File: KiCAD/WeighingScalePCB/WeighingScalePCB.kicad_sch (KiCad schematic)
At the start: 42 parts, among them J1 Conn_01x04_Pin, Q1 MMBT2222A, Q2 BSS138, Q3 BSS138, T1 TouchPad, T2 TouchPad, U1 XIAO-ESP32-S3-SMD, U2 HX711, U3 SSD1306, U4 RT9193-33GB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

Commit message: updated connectors, added chip en circuit
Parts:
- removed C10, C13, C8, C9: 1uF, Capacitor_SMD:C_0402_1005Metric, symbol Device:C
- removed C11, C12, C14: 10uF, Capacitor_SMD:C_0402_1005Metric, symbol Device:C
- removed JP1: SolderJumper_2_Bridged, symbol Jumper:SolderJumper_2_Bridged
- removed Q2, Q3: BSS138, Package_TO_SOT_SMD:SOT-23, symbol Transistor_FET:BSS138
- removed R12: 1K, Resistor_SMD:R_0402_1005Metric, symbol Device:R_US
- removed U3: SSD1306, KiCad-SSD1306_OLED-0.91-128x32-master:SSD1306_OLED-0.91-128x32, symbol SSD1306_OLED-0.91-128x32:SSD1306
- removed U4: RT9193-33GB, RT9193-33GB:SOT94P279X129-5N, symbol RT9193-33GB:RT9193-33GB
- added C17: 0.1uF, Capacitor_SMD:C_0402_1005Metric, symbol Device:C
- added D1: SP720ABTG, SOIC127P600X175-16N, symbol ESD diode:SP720ABTG
- added IC1: MAX6675ISA+T, SOIC127P600X175-8N, symbol MAX6675ISA+T:MAX6675ISA+T
- added IC2: APS11753KMDALX-9PL5, SOT95P240X115-3N, symbol APS11753KMDALX-9PL5:APS11753KMDALX-9PL5
- added J2: AudioJack4, symbol Connector_Audio:AudioJack4
- added J3: CONN_14_FFC/FPC, symbol Connector_Generic_MountingPin:Conn_01x14_MountingPin
- added J4: Battery Conn, symbol Connector:Conn_01x02_Pin
- added JP2: SolderJumper_2_Open, symbol Jumper:SolderJumper_2_Open
- added JP3: rate setting, symbol Jumper:SolderJumper_3_Open
- added Q2, Q3: NX138AKR, SOT95P230X110-3N, symbol NX138AKR Mosfet:NX138AKR
- R10, R9: value 10K -> 200K
- R11: value 1K -> 200K
- R6: value 100 -> 200K
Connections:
- net 3.3V is gone; now on net VCC: R7.1, R8.1
- net DOut: now also U1.7 (GPIO16_D6_TX); no longer U1.2 (GPIO1_A1_D1)
- net GND: now also R10.2, R9.2, C17.1, D1.8 (V-), IC1.1 (GND), IC2.3 (GND), JP2.2 (B), JP3.2 (C); no longer R11.2, R6.2
- net PD_SCK: now also U1.11 (GPIO18_D10_MOSI); no longer U1.1 (GPIO0_A0_D0)
- net VCC: now also U1.12 (3V3), C17.2, D1.16 (V+), IC1.4 (VCC), IC2.1 (VCC); no longer R10.1, R11.1, R9.1, U1.14 (5V)
- net at R3.1: now also JP3.1 (A); no longer U2.15 (RATE)
- net SO: now reaches U1.10 (GPIO20_D9_MISO)
- net SO: now also IC1.7 (SO)
- net V_BAT: now reaches U1.15 (BAT)
- net V_BAT: now also R11.1, R6.1, J4.1 (Pin_1)
- net at U1.16 (GND): now also J4.2 (Pin_2)
- net enable: now reaches U1.19 (CHIP_EN)
- net enable: now also Q2.2 (S), Q3.2 (S)
- net CS_N: now reaches U1.8 (GPIO17_D7_RX)
- net CS_N: now also IC1.6 (~{CS})
- net SCK: now reaches U1.9 (GPIO19_D8_SCK)
- net SCK: now also IC1.5 (SCK)
- net SCL_3.3V renamed SCL
- net SCL: now also U1.6 (GPIO23_D5_SCL)
- removed net SCL_5V: R9.2, U1.6 (GPIO23_D5_SCL)
- net SDA_3.3V renamed SDA
- net SDA: now also U1.5 (GPIO22_D4_SDA)
- removed net SDA_5V: R10.2, U1.5 (GPIO22_D4_SDA)
- new net: IC1.2 (T-), J2.R2, J2.T
- new net: IC1.3 (T+), J2.R1, J2.S
- new net: IC1.8 (N.C.), JP2.1 (A)
- new net: Q2.3 (D), Q3.3 (D), R11.2
- new net: IC2.2 (VOUT), Q3.1 (G), R10.1
- new net: R6.2, R9.1, U1.1 (GPIO0_A0_D0)
- new net: JP3.3 (B), U2.15 (RATE)
- new net ble_keep_awake: Q2.1 (G), U1.2 (GPIO1_A1_D1)
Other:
- note added: "Add a circuit which outputs a trigger to operate buzzer for a specific time delay for every rising edge"
- note added: "MAX6675 ~ 0.3V - 6V"
- moved on the sheet: R3, R7, R8, T1, T2

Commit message: 1. Added buzzer beep implementation - to be reviewed and calculations to be finalised 2. cleaned up schematic 3. added comments of pending activities
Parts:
- added C8, C9: 22pF, Capacitor_SMD:C_0402_1005Metric, symbol Device:C
- added D2: D, symbol Device:D
- added Q4: NX138AKR, SOT95P230X110-3N, symbol NX138AKR Mosfet:NX138AKR
- added R12, R13: 200K, Resistor_SMD:R_0402_1005Metric, symbol Device:R_US
- added U3: NE555D, Package_SO:SOIC-8_3.9x4.9mm_P1.27mm, symbol Timer:NE555D
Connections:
- net Time is gone; now on net Tare: U1.4 (GPIO21_D3), U6.1 (Q)
- net GND: now also J3.MP (MountPin), C8.2, C9.2, Q4.2 (S), U3.1 (GND)
- net Tare: now also D2.2 (A)
- net VCC: now also R12.1, R13.2, U3.8 (VCC)
- net beep: now also U3.3 (Q)
- net at D1.1 (IN_1): now also J3.1 (Pin_1)
- net at D1.10 (IN_9): now also J3.9 (Pin_9)
- net at D1.11 (IN_10): now also J3.10 (Pin_10)
- net at D1.12 (IN_11): now also J3.11 (Pin_11)
- net at D1.13 (IN_12): now also J3.12 (Pin_12)
- net at D1.14 (IN_13): now also J3.13 (Pin_13)
- net at D1.15 (IN_14): now also J3.14 (Pin_14)
- net at D1.2 (IN_2): now also J3.2 (Pin_2)
- net at D1.3 (IN_3): now also J3.3 (Pin_3)
- net at D1.4 (IN_4): now also J3.4 (Pin_4)
- net at D1.5 (IN_5): now also J3.5 (Pin_5)
- net at D1.6 (IN_6): now also J3.6 (Pin_6)
- net at D1.7 (IN_7): now also J3.7 (Pin_7)
- net at D1.9 (IN_8): now also J3.8 (Pin_8)
- new net: D2.1 (K), Q4.1 (G)
- new net: R13.1, U3.4 (R)
- new net: C9.1, R12.2, U3.6 (THR), U3.7 (DIS)
- new net: Q4.3 (D), U3.2 (TR)
- new net: C8.1, U3.5 (CV)
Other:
- note added: "Load cell amplifier"
- note added: "OLED interface"
- note added: "Processor"
- note added: "Thermocouple amplifier"
- note added: "Touch pad input and buzzer"
- note added: "slide enable implementation"
- moved on the sheet: C1, C15, C16, C17, C2, C3, C4, C5, C6, C7, D1, IC1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

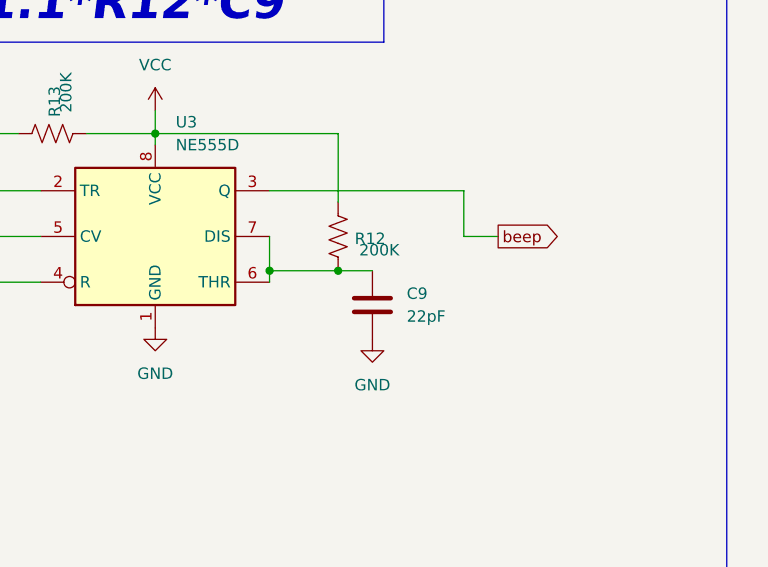
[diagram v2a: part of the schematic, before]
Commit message: Added half millisecond beep
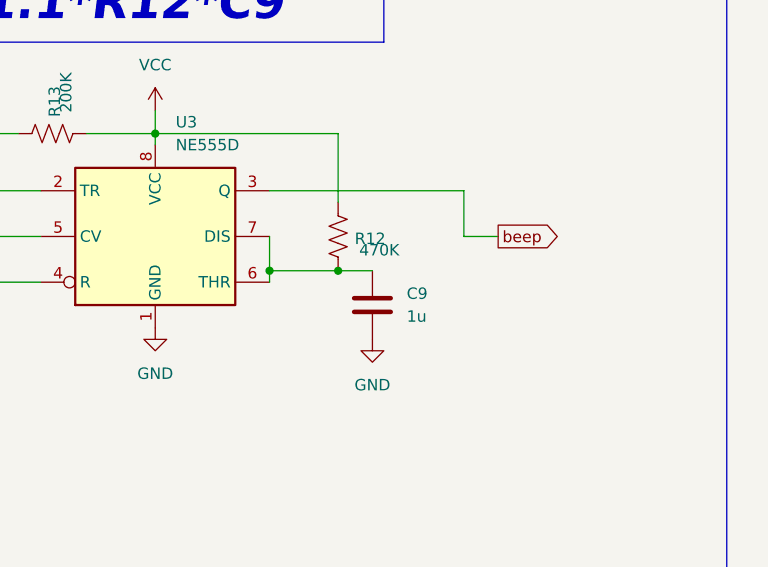
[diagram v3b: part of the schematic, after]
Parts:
- C9: value 22pF -> 1u
- R12: value 200K -> 470K
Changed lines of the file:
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@@
 			)
 		)
-		(property "Value" "22pF"
+		(property "Value" "1u"
 			(at 365.76 194.31 0)
 			(effects
@@
 			)
 		)
-		(property "Value" "200K"
+		(property "Value" "470K"
 			(at 362.712 186.944 0)
 			(effects

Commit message: Added notes for buzzer ckt added design note for hx711
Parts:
- added D3, D4, D5, D6, D7: PESD3V3U1UL, Diode_SMD:D_SOD-882, symbol Diode:PESD3V3U1UL
- C8: value 22pF -> 0.1u
- R10: value 200K -> 1K
- R13: value 200K -> 10K
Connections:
- net GND: now also D3.2 (A), D4.2 (A), D5.2 (A), D6.2 (A), D7.2 (A)
- net beep: now also D5.1 (K)
- net at IC1.2 (T-), J2.R2, J2.T: now also D6.1 (K)
- net at IC1.3 (T+), J2.R1, J2.S: now also D7.1 (K)
- net at C16.1, T2.1 (Pad), U6.3 (I): now also D4.1 (K)
- net at C15.1, T1.1 (Pad), U5.3 (I): now also D3.1 (K)
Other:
- note added: "beep ckt tbd"
- note removed: "Add a circuit which outputs a trigger to operate buzzer for a specific time delay for every rising edge"
- moved on the sheet: T2

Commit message: Added touch pad implementation
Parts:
- removed D2: D, symbol Device:D
- added C10, C11: 0.1u, Capacitor_SMD:C_0402_1005Metric, symbol Device:C
- added D2: 1N4148WT, Diode_SMD:D_SOD-523, symbol Diode:1N4148WT
- added J5: buzzer conn, symbol Connector:Conn_01x02_Pin
- added Q5: NX138AKR, SOT95P230X110-3N, symbol NX138AKR Mosfet:NX138AKR
- added R14, R15: R_US, symbol Device:R_US
- added U4: 74AHC1G08, symbol 74xGxx:74AHC1G08
- added U7: 74LVC1G79, symbol 74xGxx:74LVC1G79
- added U8: 74LVC1G04, symbol 74xGxx:74LVC1G04
- added U9: NE555D, Package_SO:SOIC-8_3.9x4.9mm_P1.27mm, symbol Timer:NE555D
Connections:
- net GND: now also U4.3 (GND), U7.3 (GND), U8.3 (GND)
- net Tare: now also D2.2 (A)
- net VCC: now also J5.2 (Pin_2), R14.1, U4.5 (VCC), U7.5 (VCC), U8.5 (VCC), U9.4 (R), U9.8 (VCC)
- net buzzer trigger: now reaches Q4.1 (G)
- net buzzer trigger: now also U4.4
- net beep: no longer names the net of D5.1 (K), U3.3 (Q)
- net beep: now also Q5.1 (G)
- new net: C10.2, C11.2, U9.1 (GND)
- new net: R14.2, R15.1, U9.7 (DIS)
- new net: C11.1, U9.5 (CV)
- new net: U4.1, U8.4
- new net: D2.1 (K), U4.2, U7.1 (D)
- new net: J5.1 (Pin_1), Q5.3 (D)
- new net: U7.4 (Q), U8.2
- new net buzzer clk: U7.2 (C), U9.3 (Q)
- new net trigg: C10.1, R15.2, U9.2 (TR), U9.6 (THR)
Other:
- moved on the sheet: C1, C15, C16, C17, C2, C3, C4, C5, C6, C7, C8, C9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

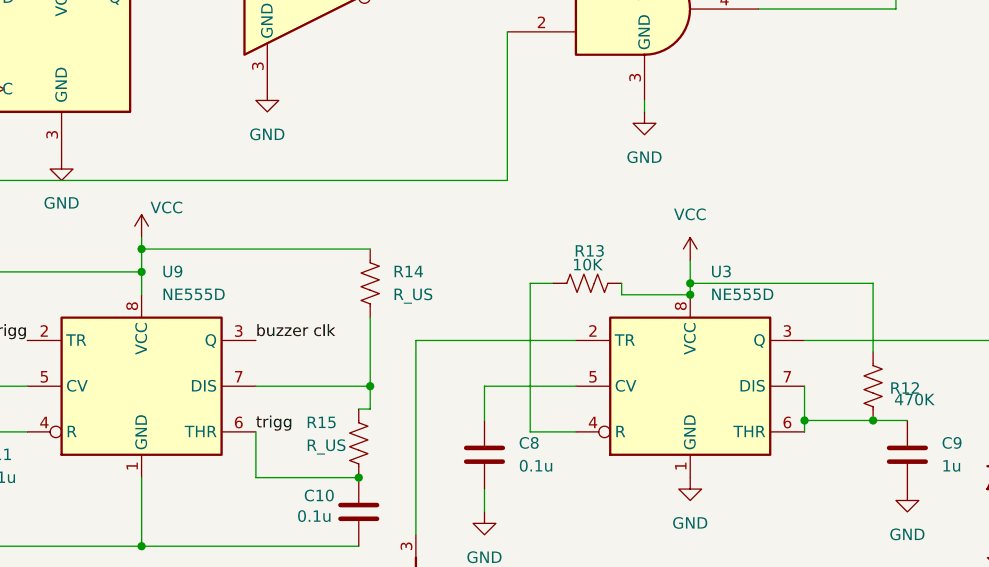
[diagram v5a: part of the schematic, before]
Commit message: replaced ne555 with lmc555 since we are operating at 3.3v
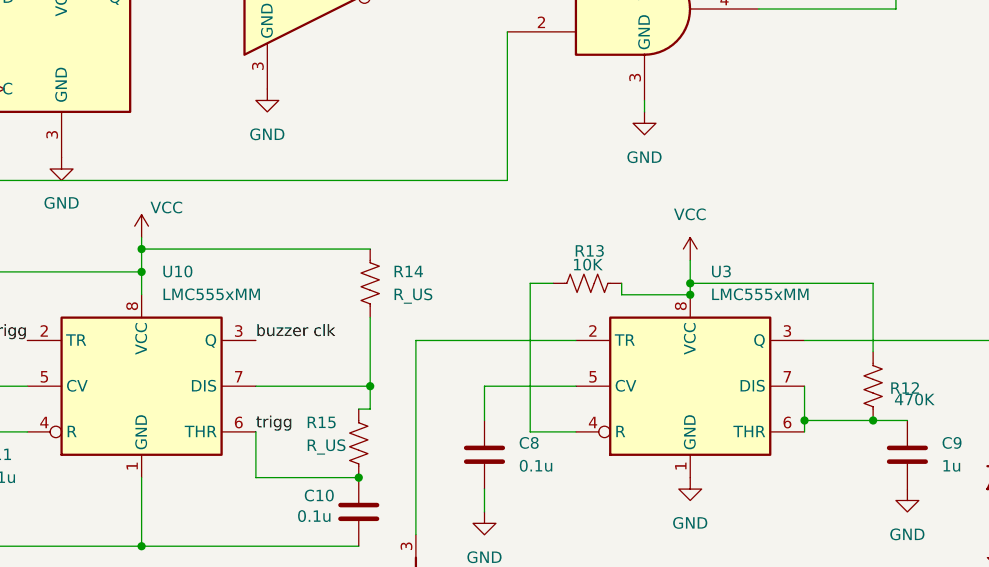
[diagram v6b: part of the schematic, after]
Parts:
- removed U3, U9: NE555D, Package_SO:SOIC-8_3.9x4.9mm_P1.27mm, symbol Timer:NE555D
- added U10, U3: LMC555xMM, Package_SO:VSSOP-8_3x3mm_P0.65mm, symbol Timer:LMC555xMM
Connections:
- net GND: now also U3.1 (GND)
- net VCC: now also U10.4 (R), U10.8 (VCC), U3.8 (VCC)
- net buzzer clk: now also U10.3 (Q)
- net trigg: now also U10.2 (TR), U10.6 (THR)
- net at C10.2, C11.2: now also U10.1 (GND)
- net at R14.2, R15.1: now also U10.7 (DIS)
- net at R13.1: now also U3.4 (R)
- net at C11.1: now also U10.5 (CV)
- net at D5.1 (K), Q5.1 (G): now also U3.3 (Q)
- net at C9.1, R12.2: now also U3.6 (THR), U3.7 (DIS)
- net at Q4.3 (D): now also U3.2 (TR)
- net at C8.1: now also U3.5 (CV)
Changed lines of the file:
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@@
 	)
 	(junction
-		(at 334.01 175.26)
-		(diameter 0)
-		(color 0 0 0 0)
-	)
-	(junction
 		(at 102.87 39.37)
 		(diameter 0)
@@
 	)
 	(junction
+		(at 334.01 175.26)
+		(diameter 0)
+		(color 0 0 0 0)
+	)
+	(junction
 		(at 208.28 187.96)
 		(diameter 0)
@@
 	)
 	(symbol
-		(lib_id "Timer:NE555D")
-		(at 273.05 185.42 0)
-		(unit 1)
-		(exclude_from_sim no)
-		(in_bom yes)
-		(on_board yes)
-		(dnp no)
-		(fields_autoplaced yes)
-		(property "Reference" "U9"
-			(at 275.3176 172.72 0)
-			(effects
-				(font
-					(size 1.27 1.27)
-				)
-				(justify left)
-			)
-		)
-		(property "Value" "NE555D"
-			(at 275.3176 175.26 0)
-			(effects
-				(font
-					(size 1.27 1.27)
-				)
-				(justify left)
-			)
-		)
-		(property "Footprint" "Package_SO:SOIC-8_3.9x4.9mm_P1.27mm"
-			(at 294.64 195.58 0)
-			(effects
-				(font
-					(size 1.27 1.27)
-				)
-				(hide yes)
-			)
-		)
-		(property "Datasheet" "http://www.ti.com/lit/ds/symlink/ne555.pdf"
-			(at 294.64 195.58 0)
-			(effects
-				(font
-					(size 1.27 1.27)
-				)
-				(hide yes)
-			)
-		)
-		(property "Description" "Precision Timers, 555 compatible, SOIC-8"
-			(at 273.05 185.42 0)
-			(effects
-				(font
-					(size 1.27 1.27)
-				)
-				(hide yes)
-			)
-		)
-		(pin "6"
-		)
-		(pin "7"
-		)
-		(pin "3"
-		)
-		(pin "4"
-		)
-		(pin "5"
-		)
-		(pin "2"
-		)
-		(pin "1"
-		)
-		(pin "8"
-		)
-		(instances
-			(project "WeighingScalePCB"
-				(path "/fb3b7c1c-1dc1-4229-b305-25c6e0b4dbdc"
-					(reference "U9")
-					(unit 1)
-				)
-			)
-		)
-	)
-	(symbol
 		(lib_id "Diode:PESD3V3U1UL")
 		(at 368.3 195.58 270)
@@
 	)
 	(symbol
-		(lib_id "Timer:NE555D")
-		(at 334.01 185.42 0)
+		(lib_id "Device:R_US")
+		(at 218.44 91.44 0)
 		(unit 1)
 		(exclude_from_sim no)
@@
 		(on_board yes)
 		(dnp no)
-		(fields_autoplaced yes)
-		(property "Reference" "U3"
-			(at 336.2776 172.72 0)
+		(property "Reference" "R9"
+			(at 221.996 91.694 0)
 			(effects
 				(font
 					(size 1.27 1.27)
 				)
-				(justify left)
 			)
 		)
-		(property "Value" "NE555D"
-			(at 336.2776 175.26 0)
+		(property "Value" "200K"
+			(at 223.012 92.964 0)
 			(effects
 				(font
 					(size 1.27 1.27)
 				)
-				(justify left)
 			)
 		)
-		(property "Footprint" "Package_SO:SOIC-8_3.9x4.9mm_P1.27mm"
-			(at 355.6 195.58 0)
+		(property "Footprint" "Resistor_SMD:R_0402_1005Metric"
+			(at 219.456 91.694 90)
 			(effects
 				(font
@@
 			)
 		)
-		(property "Datasheet" "http://www.ti.com/lit/ds/symlink/ne555.pdf"
-			(at 355.6 195.58 0)
+		(property "Datasheet" "~"
+			(at 218.44 91.44 0)
 			(effects
 				(font
@@
 			)
 		)
-		(property "Description" "Precision Timers, 555 compatible, SOIC-8"
-			(at 334.01 185.42 0)
+		(property "Description" "Resistor, US symbol"
+			(at 218.44 91.44 0)
 			(effects
 				(font
@@
 			)
 		)
-		(pin "6"
-		)
-		(pin "7"
-		)
-		(pin "3"
-		)
-		(pin "4"
-		)
-		(pin "5"
-		)
-		(pin "2"
-		)
 		(pin "1"
 		)
-		(pin "8"
+		(pin "2"
 		)
 		(instances
-			(project ""
+			(project "WeighingScalePCB"
 				(path "/fb3b7c1c-1dc1-4229-b305-25c6e0b4dbdc"
-					(reference "U3")
+					(reference "R9")
 					(unit 1)
 				)
@@
 	(symbol
 		(lib_id "Device:R_US")
-		(at 218.44 91.44 0)
+		(at 38.1 157.48 0)
 		(unit 1)
 		(exclude_from_sim no)
@@
 		(on_board yes)
 		(dnp no)
-		(property "Reference" "R9"
-			(at 221.996 91.694 0)
+		(fields_autoplaced yes)
+		(property "Reference" "R7"
+			(at 40.64 156.2099 0)
 			(effects
 				(font
 					(size 1.27 1.27)
 				)
+				(justify left)
 			)
 		)
-		(property "Value" "200K"
-			(at 223.012 92.964 0)
+		(property "Value" "10K"
+			(at 40.64 158.7499 0)
 			(effects
 				(font
 					(size 1.27 1.27)
 				)
+				(justify left)
 			)
 		)
 		(property "Footprint" "Resistor_SMD:R_0402_1005Metric"
-			(at 219.456 91.694 90)
+			(at 39.116 157.734 90)
 			(effects
 				(font
@@
 		)
 		(property "Datasheet" "~"
-			(at 218.44 91.44 0)
+			(at 38.1 157.48 0)
 			(effects
 				(font
@@
 		)
 		(property "Description" "Resistor, US symbol"
-			(at 218.44 91.44 0)
+			(at 38.1 157.48 0)
 			(effects
 				(font
@@
 			(project "WeighingScalePCB"
 				(path "/fb3b7c1c-1dc1-4229-b305-25c6e0b4dbdc"
-					(reference "R9")
+					(reference "R7")
 					(unit 1)
 				)
@@
 	)
 	(symbol
-		(lib_id "Device:R_US")
-		(at 38.1 157.48 0)
+		(lib_id "Timer:LMC555xMM")
+		(at 334.01 185.42 0)
 		(unit 1)
 		(exclude_from_sim no)
@@
 		(dnp no)
 		(fields_autoplaced yes)
-		(property "Reference" "R7"
-			(at 40.64 156.2099 0)
+		(property "Reference" "U3"
+			(at 336.2776 172.72 0)
 			(effects
 				(font
@@
 			)
 		)
-		(property "Value" "10K"
-			(at 40.64 158.7499 0)
+		(property "Value" "LMC555xMM"
+			(at 336.2776 175.26 0)
 			(effects
 				(font
@@
 			)
 		)
-		(property "Footprint" "Resistor_SMD:R_0402_1005Metric"
-			(at 39.116 157.734 90)
+		(property "Footprint" "Package_SO:VSSOP-8_3x3mm_P0.65mm"
+			(at 350.52 195.58 0)
 			(effects
 				(font
@@
 			)
 		)
-		(property "Datasheet" "~"
-			(at 38.1 157.48 0)
+		(property "Datasheet" "http://www.ti.com/lit/ds/symlink/lmc555.pdf"
+			(at 355.6 195.58 0)
 			(effects
 				(font
@@
 			)
 		)
-		(property "Description" "Resistor, US symbol"
-			(at 38.1 157.48 0)
+		(property "Description" "CMOS Timer, 555 compatible, VSSOP-8"
+			(at 334.01 185.42 0)
 			(effects
 				(font
@@
 			)
 		)
-		(pin "1"
+		(pin "6"
+		)
+		(pin "7"
+		)
+		(pin "3"
+		)
+		(pin "4"
+		)
+		(pin "5"
 		)
 		(pin "2"
 		)
+		(pin "1"
+		)
+		(pin "8"
+		)
 		(instances
 			(project "WeighingScalePCB"
 				(path "/fb3b7c1c-1dc1-4229-b305-25c6e0b4dbdc"
-					(reference "R7")
+					(reference "U3")
 					(unit 1)
 				)
@@
 					(unit 1)
 				)
+			)
+		)
+	)
+	(symbol
+		(lib_id "Timer:LMC555xMM")
+		(at 273.05 185.42 0)
+		(unit 1)
+		(exclude_from_sim no)
+		(in_bom yes)
+		(on_board yes)
+		(dnp no)
+		(fields_autoplaced yes)
+		(property "Reference" "U10"
+			(at 275.3176 172.72 0)
+			(effects
+				(font
+					(size 1.27 1.27)
+				)
+				(justify left)
+			)
+		)
+		(property "Value" "LMC555xMM"
+			(at 275.3176 175.26 0)
+			(effects
+				(font
+					(size 1.27 1.27)
+				)
+				(justify left)
+			)
+		)
+		(property "Footprint" "Package_SO:VSSOP-8_3x3mm_P0.65mm"
+			(at 289.56 195.58 0)
+			(effects
+				(font
+					(size 1.27 1.27)
+				)
+				(hide yes)
+			)
+		)
+		(property "Datasheet" "http://www.ti.com/lit/ds/symlink/lmc555.pdf"
+			(at 294.64 195.58 0)
+			(effects
+				(font
+					(size 1.27 1.27)
+				)
+				(hide yes)
+			)
+		)
+		(property "Description" "CMOS Timer, 555 compatible, VSSOP-8"
+			(at 273.05 185.42 0)
+			(effects
+				(font
+					(size 1.27 1.27)
+				)
+				(hide yes)
+			)
+		)
+		(pin "6"
+		)
+		(pin "7"
+		)
+		(pin "3"
+		)
+		(pin "4"
+		)
+		(pin "5"
+		)
+		(pin "2"
+		)
+		(pin "1"
+		)
+		(pin "8"
+		)
+		(instances
+			(project ""
+				(path "/fb3b7c1c-1dc1-4229-b305-25c6e0b4dbdc"
+					(reference "U10")
+					(unit 1)
+				)
